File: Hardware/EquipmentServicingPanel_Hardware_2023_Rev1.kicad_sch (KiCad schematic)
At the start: 42 parts, among them U1 Raspberry_Pi, U2 OKI, U3 TSR_1-2450

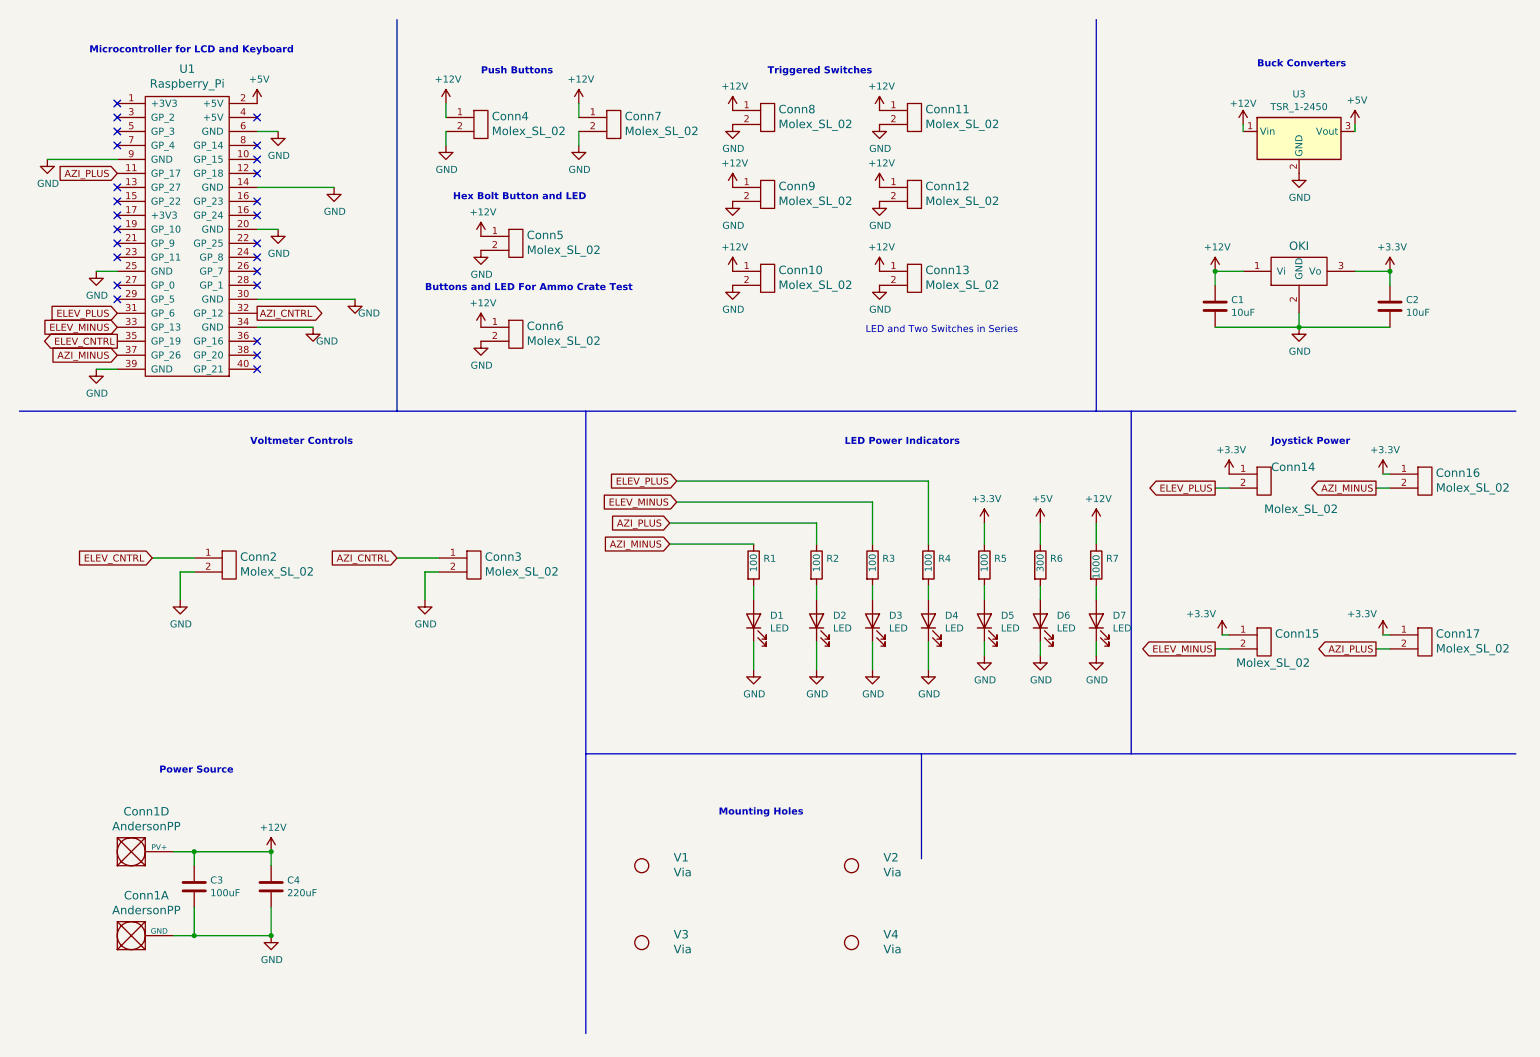
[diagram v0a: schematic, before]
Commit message: schematic work
Almost finished, still needs work on potentiometer
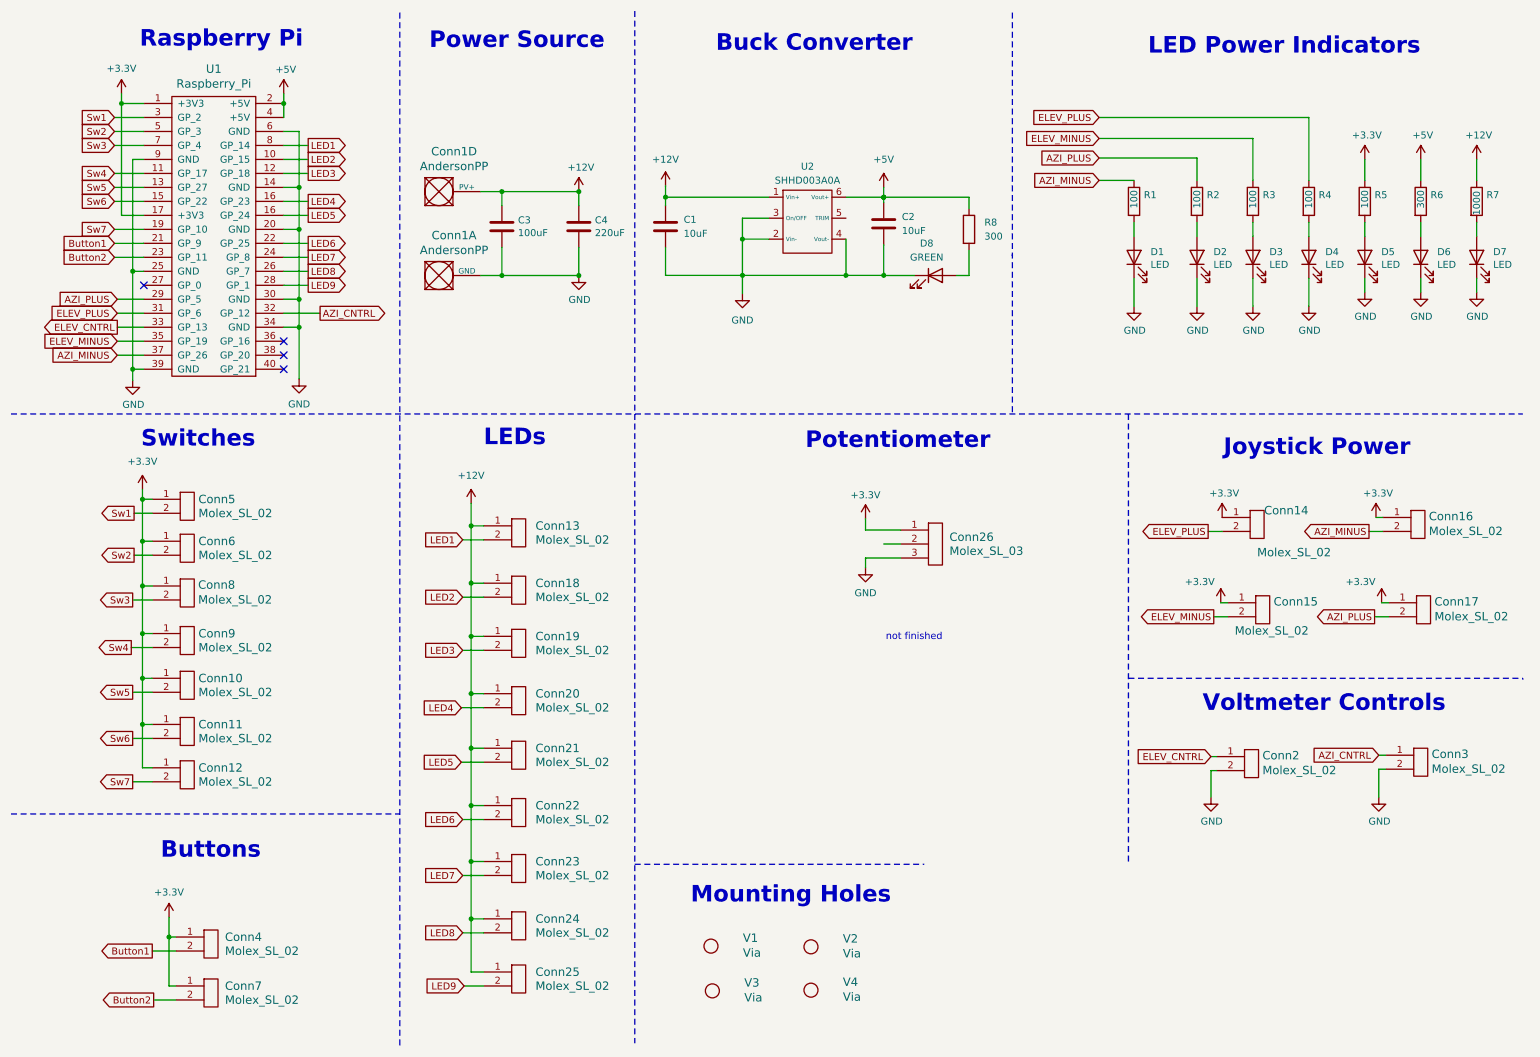
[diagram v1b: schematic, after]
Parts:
- removed U2: OKI, MRDT_Devices:OKI_Horizontal, symbol MRDT_Devices:OKI
- removed U3: TSR_1-2450, MRDT_Devices:TSR_1-2433, symbol Regulator_Switching:TSR_1-2450
- added Conn18, Conn19, Conn20, Conn21, Conn22, Conn23, Conn24, Conn25: Molex_SL_02, symbol MRDT_Connectors:Molex_SL_02
- added Conn26: Molex_SL_03, symbol MRDT_Connectors:Molex_SL_03
- added D8: GREEN, symbol Device:LED
- added R8: 300, symbol Device:R
- added U2: SHHD003A0A, MRDT_Devices:SHHD003A0A-SRZ, symbol MRDT_Devices:SHHD003A0A
- C1, C2: footprint Capacitor_SMD:C_0603_1608Metric_Pad1.08x0.95mm_HandSolder -> (none)
- Conn10, Conn11, Conn12, Conn13, Conn9: footprint MRDT_Connectors:MOLEX_SL_02_Vertical -> (none)
- Conn4, Conn5, Conn6, Conn7: footprint MRDT_Connectors:MOLEX_SL_02_Horizontal -> (none)
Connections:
- net +12V: now also Conn18.1, Conn19.1, Conn20.1, Conn21.1, Conn22.1, Conn23.1, Conn24.1, Conn25.1, U2.1 (Vin+); no longer Conn10.1, Conn11.1, Conn12.1, Conn4.1, Conn5.1, Conn6.1, Conn7.1, Conn8.1, Conn9.1
- net +3V3: no longer C2.1
- net +5V: now also C2.1, U1.4 (+5V), R8.1, U2.6 (Vout+)
- net AZI_PLUS: now also U1.29 (GP_5); no longer U1.11 (GP_17)
- net ELEV_CNTRL: now also U1.33 (GP_13); no longer U1.35 (GP_19)
- net ELEV_MINUS: now also U1.35 (GP_19); no longer U1.33 (GP_13)
- net GND: now also Conn26.3, D8.1 (K), U2.2 (Vin-), U2.3 (On/OFF), U2.4 (Vout-); no longer Conn10.2, Conn11.2, Conn12.2, Conn13.2, Conn4.2, Conn5.2, Conn6.2, Conn7.2, Conn8.2, Conn9.2
- net +3.3V: now reaches U1.1 (+3V3)
- net +3.3V: now also Conn10.1, Conn11.1, Conn12.1, Conn4.1, Conn5.1, Conn6.1, Conn7.1, Conn8.1, Conn9.1, U1.17 (+3V3), Conn26.1
- net LED2: now reaches U1.10 (GP_15)
- net LED2: now also Conn18.2
- net LED3: now reaches U1.12 (GP_18)
- net LED3: now also Conn19.2
- net Sw5: now reaches U1.13 (GP_27)
- net Sw5: now also Conn10.2
- net Sw6: now reaches U1.15 (GP_22)
- net Sw6: now also Conn11.2
- net LED5: now reaches U1.16 (GP_24)
- net LED5: now also Conn21.2
- net Sw7: now reaches U1.19 (GP_10)
- net Sw7: now also Conn12.2
- net Button1: now reaches U1.21 (GP_9)
- net Button1: now also Conn4.2
- net LED6: now reaches U1.22 (GP_25)
- net LED6: now also Conn22.2
- net Button2: now reaches U1.23 (GP_11)
- net Button2: now also Conn7.2
- net LED7: now reaches U1.24 (GP_8)
- net LED7: now also Conn23.2
- net LED8: now reaches U1.26 (GP_7)
- net LED8: now also Conn24.2
- net LED9: now reaches U1.28 (GP_1)
- net LED9: now also Conn25.2
- net Sw1: now reaches U1.3 (GP_2)
- net Sw1: now also Conn5.2
- net Sw2: now reaches U1.5 (GP_3)
- net Sw2: now also Conn6.2
- net Sw3: now reaches U1.7 (GP_4)
- net Sw3: now also Conn8.2
- net LED1: now reaches U1.8 (GP_14)
- net LED1: now also Conn13.2
- new net: D8.2 (A), R8.2
- new net LED4: Conn20.2, U1.16 (GP_24)
- new net Sw4: Conn9.2, U1.11 (GP_17)
- no-connect marks 25 -> 4
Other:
- note added: "Buck Converter"
- note added: "Buttons"
- note added: "LEDs"
- note added: "Potentiometer"
- note added: "Raspberry Pi"
- note added: "Switches"
- note added: "not finished"
- note removed: "Buck Converters"
- note removed: "Buttons and LED For Ammo Crate Test"
- note removed: "Hex Bolt Button and LED"
- note removed: "LED and Two Switches in Series"
- note removed: "Microcontroller for LCD and Keyboard"
- note removed: "Push Buttons"
- note removed: "Triggered Switches"
- moved on the sheet: C3, C4, Conn14, Conn15, Conn16, Conn17, Conn1A, Conn1D, Conn2, Conn3, Conn8, D1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
